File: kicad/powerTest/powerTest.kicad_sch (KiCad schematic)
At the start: 40 parts, among them J1 Solar Panel, J10 Conn_01x01_Pin, J11 Conn_01x01_Pin, J2 BATT, J3 3V3 Sensor Bus, J4 Conn_01x01_Pin, J5 Conn_01x01_Pin, J6 Conn_01x01_Pin, J7 Conn_01x01_Pin, J8 Conn_01x01_Pin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

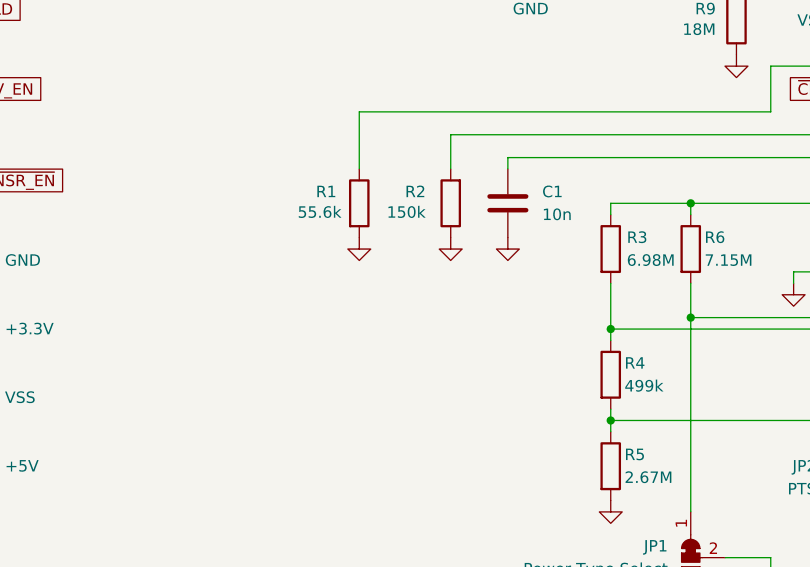
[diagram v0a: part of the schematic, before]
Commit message: Power Board Test 1.1
Updated Test Power Board
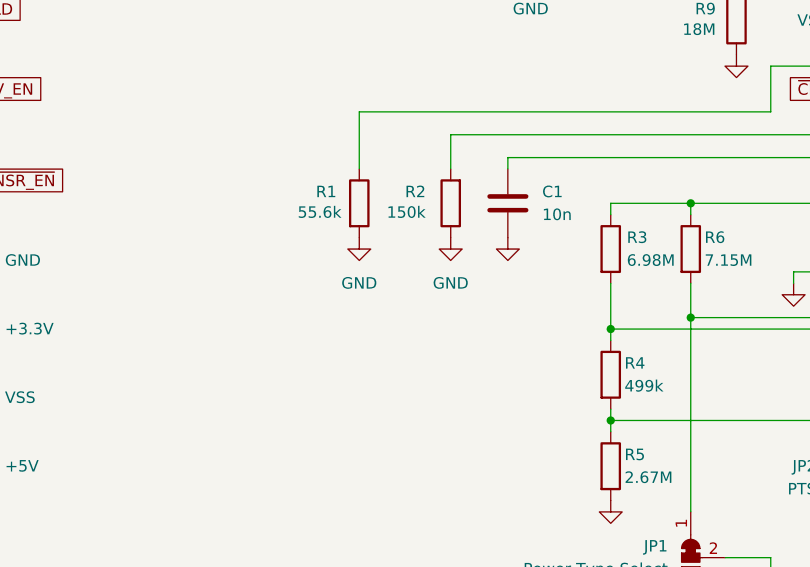
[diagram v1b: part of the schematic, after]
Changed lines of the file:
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@@
+	)
+	(symbol
+		(lib_id "power:GND")
+		(at 101.6 104.14 0)
+		(unit 1)
+		(exclude_from_sim no)
+		(in_bom yes)
+		(on_board yes)
+		(dnp no)
+		(fields_autoplaced yes)
+		(property "Reference" "#PWR01"
+			(at 101.6 110.49 0)
+			(effects
+				(font
+					(size 1.27 1.27)
+				)
+				(hide yes)
+			)
+		)
+		(property "Value" "GND"
+			(at 101.6 109.22 0)
+			(effects
+				(font
+					(size 1.27 1.27)
+				)
+			)
+		)
+		(property "Footprint" ""
+			(at 101.6 104.14 0)
+			(effects
+				(font
+					(size 1.27 1.27)
+				)
+				(hide yes)
+			)
+		)
+		(property "Datasheet" ""
+			(at 101.6 104.14 0)
+			(effects
+				(font
+					(size 1.27 1.27)
+				)
+				(hide yes)
+			)
+		)
+		(property "Description" "Power symbol creates a global label with name \"GND\" , ground"
+			(at 101.6 104.14 0)
+			(effects
+				(font
+					(size 1.27 1.27)
+				)
+				(hide yes)
+			)
+		)
+		(pin "1"
+		)
+		(instances
+			(project "powerTest"
+				(path "/f735e6f2-93a3-4f3f-a144-2721d2749039"
+					(reference "#PWR01")
+					(unit 1)
+				)
+			)
+		)
 	)
 	(symbol
@@
 	)
 	(symbol
-		(lib_id "power:GND")
-		(at 101.6 104.14 0)
-		(unit 1)
-		(exclude_from_sim no)
-		(in_bom yes)
-		(on_board yes)
-		(dnp no)
-		(fields_autoplaced yes)
-		(property "Reference" "#PWR02"
-			(at 101.6 110.49 0)
-			(effects
-				(font
-					(size 1.27 1.27)
-				)
-				(hide yes)
-			)
-		)
-		(property "Value" "GND"
-			(at 101.6 109.22 0)
-			(effects
-				(font
-					(size 1.27 1.27)
-				)
-				(hide yes)
-			)
-		)
-		(property "Footprint" ""
-			(at 101.6 104.14 0)
-			(effects
-				(font
-					(size 1.27 1.27)
-				)
-				(hide yes)
-			)
-		)
-		(property "Datasheet" ""
-			(at 101.6 104.14 0)
-			(effects
-				(font
-					(size 1.27 1.27)
-				)
-				(hide yes)
-			)
-		)
-		(property "Description" "Power symbol creates a global label with name \"GND\" , ground"
-			(at 101.6 104.14 0)
-			(effects
-				(font
-					(size 1.27 1.27)
-				)
-				(hide yes)
-			)
-		)
-		(pin "1"
-		)
-		(instances
-			(project "powerTest"
-				(path "/f735e6f2-93a3-4f3f-a144-2721d2749039"
-					(reference "#PWR02")
-					(unit 1)
-				)
-			)
-		)
-	)
-	(symbol
 		(lib_id "Device:R")
 		(at 133.35 80.01 180)
@@
 				(path "/f735e6f2-93a3-4f3f-a144-2721d2749039"
 					(reference "#PWR018")
+					(unit 1)
+				)
+			)
+		)
+	)
+	(symbol
+		(lib_id "power:GND")
+		(at 91.44 104.14 0)
+		(unit 1)
+		(exclude_from_sim no)
+		(in_bom yes)
+		(on_board yes)
+		(dnp no)
+		(fields_autoplaced yes)
+		(property "Reference" "#PWR030"
+			(at 91.44 110.49 0)
+			(effects
+				(font
+					(size 1.27 1.27)
+				)
+				(hide yes)
+			)
+		)
+		(property "Value" "GND"
+			(at 91.44 109.22 0)
+			(effects
+				(font
+					(size 1.27 1.27)
+				)
+			)
+		)
+		(property "Footprint" ""
+			(at 91.44 104.14 0)
+			(effects
+				(font
+					(size 1.27 1.27)
+				)
+				(hide yes)
+			)
+		)
+		(property "Datasheet" ""
+			(at 91.44 104.14 0)
+			(effects
+				(font
+					(size 1.27 1.27)
+				)
+				(hide yes)
+			)
+		)
+		(property "Description" "Power symbol creates a global label with name \"GND\" , ground"
+			(at 91.44 104.14 0)
+			(effects
+				(font
+					(size 1.27 1.27)
+				)
+				(hide yes)
+			)
+		)
+		(pin "1"
+		)
+		(instances
+			(project "powerTest"
+				(path "/f735e6f2-93a3-4f3f-a144-2721d2749039"
+					(reference "#PWR030")
 					(unit 1)
 				)
@@
 					(unit 1)
 				)
-			)
-		)
-	)
-	(symbol
-		(lib_id "power:GND")
-		(at 91.44 104.14 0)
-		(unit 1)
-		(exclude_from_sim no)
-		(in_bom yes)
-		(on_board yes)
-		(dnp no)
-		(fields_autoplaced yes)
-		(property "Reference" "#PWR01"
-			(at 91.44 110.49 0)
-			(effects
-				(font
-					(size 1.27 1.27)
-				)
-				(hide yes)
-			)
-		)
-		(property "Value" "GND"
-			(at 91.44 109.22 0)
-			(effects
-				(font
-					(size 1.27 1.27)
-				)
-				(hide yes)
-			)
-		)
-		(property "Footprint" ""
-			(at 91.44 104.14 0)
-			(effects
-				(font
-					(size 1.27 1.27)
-				)
-				(hide yes)
-			)
-		)
-		(property "Datasheet" ""
-			(at 91.44 104.14 0)
-			(effects
-				(font
-					(size 1.27 1.27)
-				)
-				(hide yes)
-			)
-		)
-		(property "Description" "Power symbol creates a global label with name \"GND\" , ground"
-			(at 91.44 104.14 0)
-			(effects
-				(font
-					(size 1.27 1.27)
-				)
-				(hide yes)
-			)
-		)
-		(pin "1"
-		)
-		(instances
-			(project "powerTest"
-				(path "/f735e6f2-93a3-4f3f-a144-2721d2749039"
-					(reference "#PWR01")
-					(unit 1)
-				)

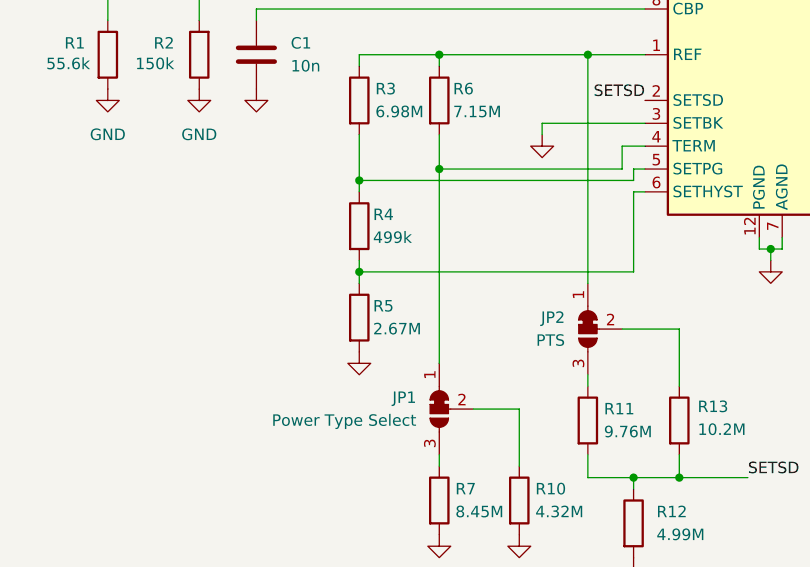
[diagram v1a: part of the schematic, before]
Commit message: power test resistor change
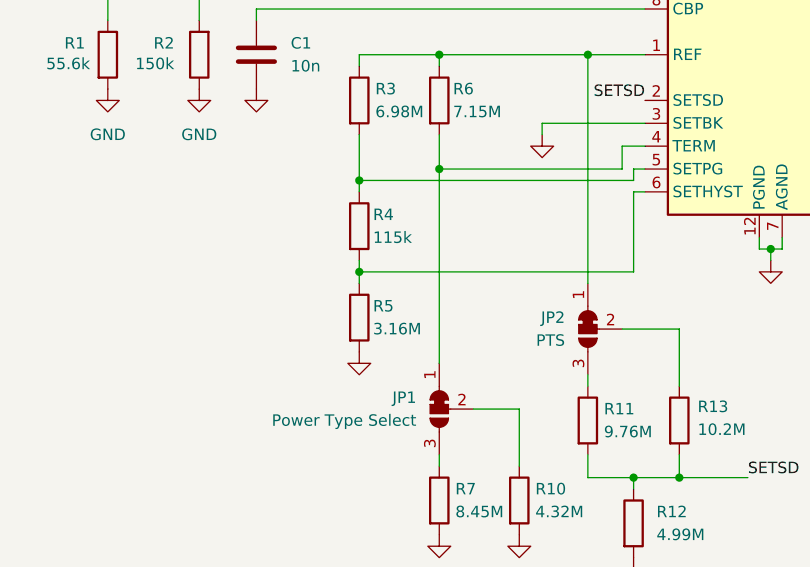
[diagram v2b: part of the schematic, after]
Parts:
- R4: value 499k -> 115k
- R5: value 2.67M -> 3.16M
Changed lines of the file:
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@@
 	(label "SETSD"
 		(at 162.56 147.32 0)
-		(fields_autoplaced yes)
 		(effects
 			(font
@@
 	(label "SETSD"
 		(at 151.13 105.41 180)
-		(fields_autoplaced yes)
 		(effects
 			(font
@@
 			)
 		)
-		(property "Value" "499k"
+		(property "Value" "115k"
 			(at 120.904 120.65 0)
 			(effects
@@
 			)
 		)
-		(property "Value" "2.67M"
+		(property "Value" "3.16M"
 			(at 120.904 130.81 0)
 			(effects

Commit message: updates
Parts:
- added C7: 10u, Capacitor_SMD:C_0603_1608Metric, symbol Device:C
- added D1: 3.3V, Diode_SMD:D_0402_1005Metric_Pad0.77x0.64mm_HandSolder, symbol Device:D_Zener
- L1: footprint Inductor_SMD:L_0603_1608Metric -> Inductor_SMD:L_Vishay_IFSC-1515AH_4x4x1.8mm
- R10: value 4.32M -> 5.1M
- R11: value 9.76M -> 10M
- R12: value 4.99M -> 4.7M
- R13: value 10.2M -> 10M
- R3: value 6.98M -> 7.5M
- R5: value 3.16M -> 3.3M
- R6: value 7.15M -> 7.5M
- R7: value 8.45M -> 7.5M
- R8: value 4.7M -> 5.1M
- R9: value 18M -> 20M
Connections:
- net GND: now also C7.2, D1.2 (A)
- net at C2.1, J1.2 (Pin_2), L1.1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: now also D1.1 (K)
- net at J2.1 (Pin_1), U1.17 (BAT): now also C7.1
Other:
- moved on the sheet: J1, J2, J3, L1, Q1
